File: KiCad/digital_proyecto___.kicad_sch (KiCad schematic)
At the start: 0 parts

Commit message: Poner parte digital
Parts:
- added D1 (x2), D2 (x2), D3 (x2), D4 (x2): RF01VM2S, Diode_SMD:D_SOD-323, symbol Diode:RF01VM2S
- added D5: WS2812B, LED_SMD:LED_WS2812B_PLCC4_5.0x5.0mm_P3.2mm, symbol LED:WS2812B
- added J1 (x2): Conn_01x02, symbol Connector_Generic:Conn_01x02
- added J2, J3: DE9_Pins, symbol Connector:DE9_Pins
- added Q1, Q3 (x2), Q4: PMOS, symbol Simulation_SPICE:PMOS
- added Q1, Q2 (x2), Q4: NMOS, symbol Simulation_SPICE:NMOS
- added R1: 10k, symbol Device:R
- added R2: 330k, symbol Device:R
- added SW1, SW2: SW_SPST, symbol Switch:SW_SPST
- added U1: MCP2551-I-SN, Package_SO:SOIC-8_3.9x4.9mm_P1.27mm, symbol Interface_CAN_LIN:MCP2551-I-SN
- added U2, U3, U4, U5: 74HC04, symbol 74xx:74HC04
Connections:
- new net: Q1.2 (G), U2.2
- new net: Q2.2 (G), U4.2
- new net: Q2.2 (G), U3.2
- new net: R1.1, U1.8 (Rs)
- new net: SW1.2 (B), SW2.1 (A)
- new net: Q4.2 (G), U5.2
- new net: D5.4 (DIN), R2.1
- new net +3.3V: D5.1 (VDD), SW1.1 (A), U1.3 (VDD)
- new net CAN_H: J3.7, U1.7 (CANH)
- new net CAN_L: J3.2, U1.6 (CANL)
- new net CAN_RX: U1.4 (RXD)
- new net CAN_TX: U1.1 (TXD)
- new net GND: D1.2 (A), D2.2 (A), D2.2 (A), D4.2 (A), D5.3 (VSS), J2.5, J3.3, Q1.3 (S), Q2.3 (S), Q2.3 (S), Q4.3 (S), R1.2, U1.2 (VSS)
- new net INA1_M1: Q3.2 (G), U2.1
- new net INA2_M1: Q4.2 (G), U3.1
- new net INB1_M2: Q1.2 (G), U4.1
- new net INB2_M2: Q3.2 (G), U5.1
- new net LED_RGB: R2.2
- new net M1+: D2.1 (K), D3.2 (A), J1.2 (Pin_2), Q1.1 (D), Q3.1 (D), SW2.2 (B)
- new net M1-: D1.1 (K), D4.2 (A), J1.1 (Pin_1), Q2.1 (D), Q4.1 (D)
- new net M2+: D1.2 (A), D2.1 (K), J1.2 (Pin_2), Q1.1 (D), Q2.1 (D)
- new net M2-: D3.2 (A), D4.1 (K), J1.1 (Pin_1), Q3.1 (D), Q4.1 (D)
- new net USART_RX: J2.2
- new net USART_TX: J2.3
- new net V_bat: D1.1 (K), D3.1 (K), D3.1 (K), D4.1 (K), Q1.3 (S), Q3.3 (S), Q3.3 (S), Q4.3 (S)
- no-connect marks 0 -> 14
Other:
- note added: "CANH → DB9 pin 7 CANL → DB9 pin 2 GND → DB9 pin 3"
- note added: "H-BRIDGE 1 (M1)"
- note added: "H-BRIDGE 2 (M2)"
- note added: "LED RGB"
- note added: "Sensor Final de Carrera"
- note added: "TRANSCEIVER CAN"
- note added: "USART"

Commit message: Subida para juntarlo todo 100 por 100
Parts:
- renumbered D4 to D?, D1 to D?, D5 to D?, D2 to D?, D3 to D?, J3 to J?, J1 to J?, J2 to J?, Q3 to Q?, Q2 to Q?, Q4 to Q?, Q1 to Q?, R2 to R?, R1 to R?, SW1 to SW?, SW2 to SW?, U2 to U?, U4 to U?, U1 to U?, U3 to U?, U5 to U?
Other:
- moved on the sheet: D1, D2, D3, D4, D?, J1, J?, Q1, Q2, Q3, Q4, Q?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

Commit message: Actualización ESquematico arreglandolo y corrigiendo fallos
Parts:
- removed SW? (x2): SW_SPST, symbol Switch:SW_SPST
- added C1, C2, C3, C4, C5, C6, C7: 100n, symbol Device:C
- added R3: 120, symbol Device:R
- added R4: 10k, symbol Device:R
- added U6: MAX3232, symbol Interface_UART:MAX3232
- added U7: A1101xLH, Package_TO_SOT_SMD:SOT-23W, symbol Sensor_Magnetic:A1101xLH
- gave numbers to parts that had none: 19
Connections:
- net +3.3V: now also C1.1, C2.1, C3.1, C7.1, R4.1, U6.16 (VCC), U7.1 (V_{CC})
- net CAN_H: now also R3.1
- net CAN_L: now also R3.2
- net GND: now also C1.2, C2.2, C3.2, C7.2, U6.15 (GND), U7.3 (GND)
- net USART_RX: now also U6.13 (R1IN); no longer J2.2
- net USART_TX: now also U6.11 (T1IN); no longer J2.3
- net IN_LED: now reaches D5.4 (DIN), R2.1
- new net: C4.1, U6.1 (C1+)
- new net: C6.1, U6.2 (VS+)
- new net: C4.2, U6.3 (C1-)
- new net: C5.1, U6.4 (C2+)
- new net: C5.2, U6.5 (C2-)
- new net: C6.2, U6.6 (VS-)
- new net MAX_RX: J2.2, U6.12 (R1OUT)
- new net MAX_TX: J2.3, U6.14 (T1OUT)
- new net Sensor_Hall: R4.2, U7.2 (V_{OUT})
- no-connect marks 14 -> 19
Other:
- moved on the sheet: D5, J2, J3, R1, R2, U1

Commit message: Nuevos cambios esquemativo v3
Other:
- note added: "Cada sensor mide el campo magnetico que tiene frente a él. Como piden que el final de carrera sea para el motor del cristal (M1), habra que poner el sensor hall cerca de este motor."
- moved on the sheet: J2
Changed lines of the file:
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@@
 		)
 	)
+	(text "Cada sensor mide el campo magnetico\nque tiene frente a él. Como piden que\nel final de carrera sea para el motor\ndel cristal (M1), habra que poner el \nsensor hall cerca de este motor."
+		(exclude_from_sim no)
+		(at 187.198 42.164 0)
+		(effects
+			(font
+				(size 1.27 1.27)
+			)
+		)
+	)
 	(text "H-BRIDGE 1 (M1)\n"
 		(exclude_from_sim no)
@@
 	)
 	(no_connect
-		(at 39.37 128.27)
+		(at 45.72 130.81)
 	)
 	(no_connect
-		(at 39.37 115.57)
+		(at 45.72 118.11)
 	)
 	(no_connect
-		(at 39.37 130.81)
+		(at 45.72 133.35)
 	)
 	(no_connect
@@
 	)
 	(no_connect
-		(at 39.37 123.19)
+		(at 45.72 125.73)
 	)
 	(no_connect
@@
 	)
 	(no_connect
-		(at 39.37 113.03)
+		(at 45.72 115.57)
 	)
 	(no_connect
@@
 	)
 	(no_connect
-		(at 39.37 118.11)
+		(at 45.72 120.65)
 	)
 	(wire
@@
 	(wire
 		(pts
-			(xy 39.37 110.49) (xy 31.75 110.49)
+			(xy 45.72 113.03) (xy 53.34 113.03)
 		)
 		(stroke
@@
 	(wire
 		(pts
-			(xy 31.75 110.49) (xy 31.75 113.03)
+			(xy 53.34 113.03) (xy 53.34 115.57)
 		)
 		(stroke
@@
 	(global_label "MAX_RX"
 		(shape input)
-		(at 39.37 125.73 180)
+		(at 45.72 128.27 0)
 		(fields_autoplaced yes)
 		(effects
@@
 				(size 1.27 1.27)
 			)
-			(justify right)
+			(justify left)
 		)
 		(property "Intersheetrefs" "${INTERSHEET_REFS}"
-			(at 29.1882 125.73 0)
+			(at 55.9018 128.27 0)
 			(effects
 				(font
 					(size 1.27 1.27)
 				)
-				(justify right)
+				(justify left)
 				(hide yes)
 			)
@@
 	(global_label "MAX_TX"
 		(shape input)
-		(at 39.37 120.65 180)
+		(at 45.72 123.19 0)
 		(fields_autoplaced yes)
 		(effects
@@
 				(size 1.27 1.27)
 			)
-			(justify right)
+			(justify left)
 		)
 		(property "Intersheetrefs" "${INTERSHEET_REFS}"
-			(at 29.4906 120.65 0)
+			(at 55.5994 123.19 0)
 			(effects
 				(font
 					(size 1.27 1.27)
 				)
-				(justify right)
+				(justify left)
 				(hide yes)
 			)
@@
 	(symbol
 		(lib_id "Connector:DE9_Pins")
-		(at 46.99 120.65 0)
+		(at 38.1 123.19 0)
+		(mirror y)
 		(unit 1)
 		(exclude_from_sim no)
@@
 		(fields_autoplaced yes)
 		(property "Reference" "J2"
-			(at 52.07 119.3799 0)
+			(at 33.02 121.9199 0)
 			(effects
 				(font
@@
 		)
 		(property "Value" "DE9_Pins"
-			(at 52.07 121.9199 0)
+			(at 33.02 124.4599 0)
 			(effects
 				(font
@@
 		)
 		(property "Footprint" ""
-			(at 46.99 120.65 0)
+			(at 38.1 123.19 0)
 			(effects
 				(font
@@
 		)
 		(property "Datasheet" "~"
-			(at 46.99 120.65 0)
+			(at 38.1 123.19 0)
 			(effects
 				(font
@@
 		)
 		(property "Description" "9-pin D-SUB connector, pins (male)"
-			(at 46.99 120.65 0)
+			(at 38.1 123.19 0)
 			(effects
 				(font
@@
 	(symbol
 		(lib_id "power:GND")
-		(at 31.75 113.03 0)
+		(at 53.34 115.57 0)
+		(mirror y)
 		(unit 1)
 		(exclude_from_sim no)
@@
 		(fields_autoplaced yes)
 		(property "Reference" "#PWR09"
-			(at 31.75 119.38 0)
+			(at 53.34 121.92 0)
 			(effects
 				(font
@@
 		)
 		(property "Value" "GND"
-			(at 31.75 118.11 0)
+			(at 53.34 120.65 0)
 			(effects
 				(font
@@
 		)
 		(property "Footprint" ""
-			(at 31.75 113.03 0)
+			(at 53.34 115.57 0)
 			(effects
 				(font
@@
 		)
 		(property "Datasheet" ""
-			(at 31.75 113.03 0)
+			(at 53.34 115.57 0)
 			(effects
 				(font
@@
 		)
 		(property "Description" "Power symbol creates a global label with name \"GND\" , ground"
-			(at 31.75 113.03 0)
+			(at 53.34 115.57 0)
 			(effects
 				(font

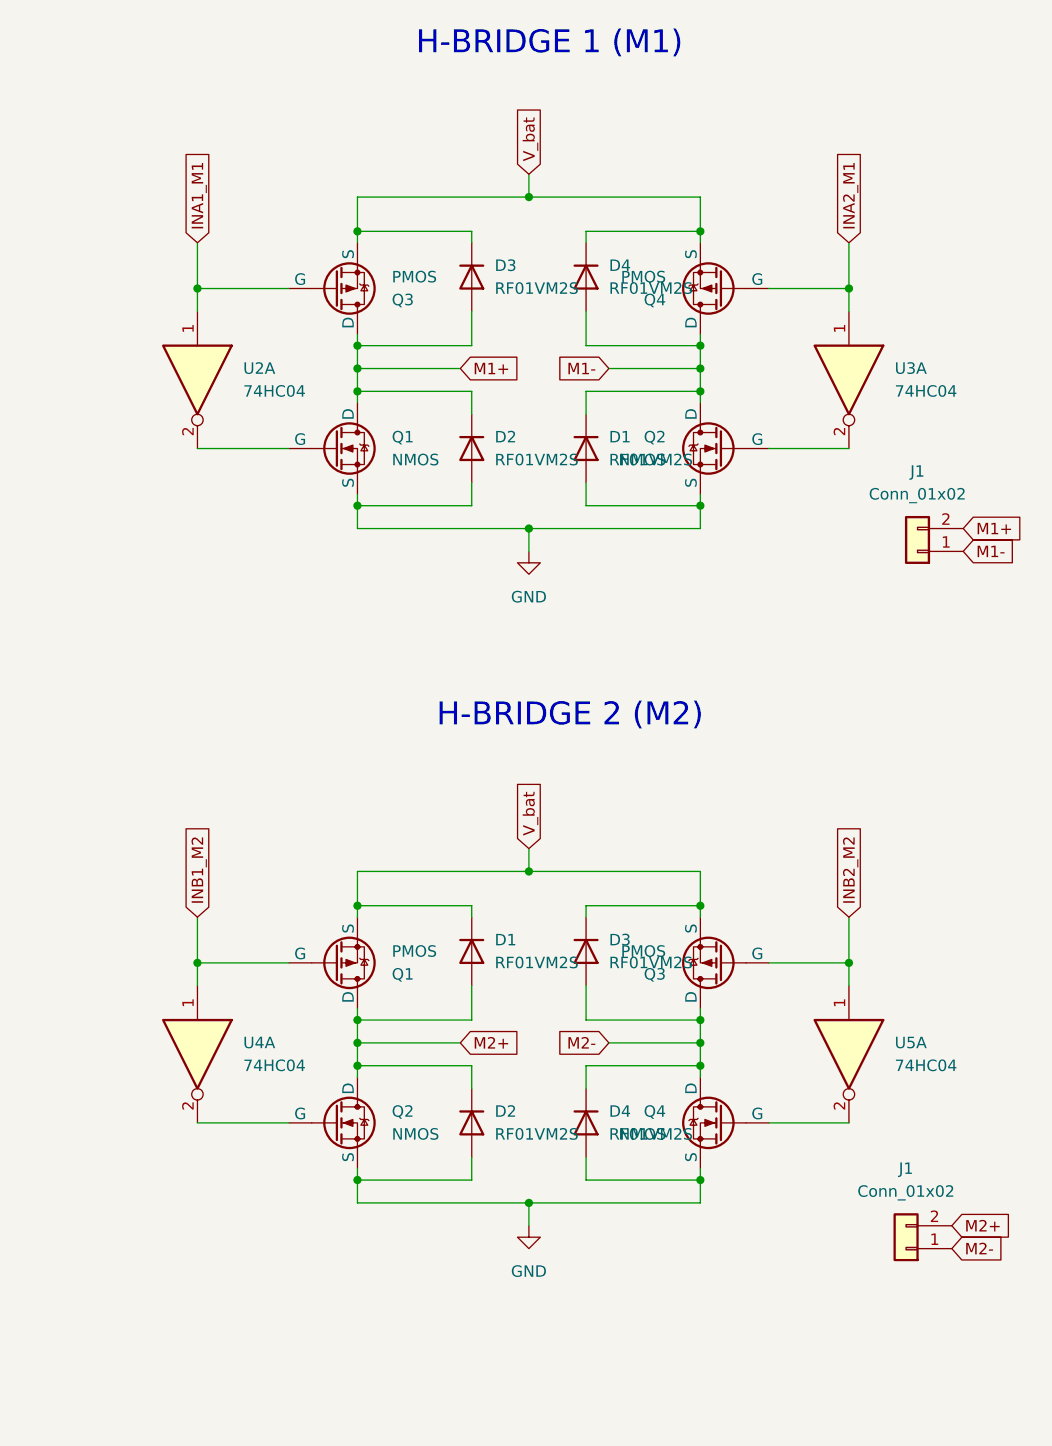
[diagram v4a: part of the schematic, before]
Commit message: Actualización de Esquematico, he puesto footprints y readme cambiado
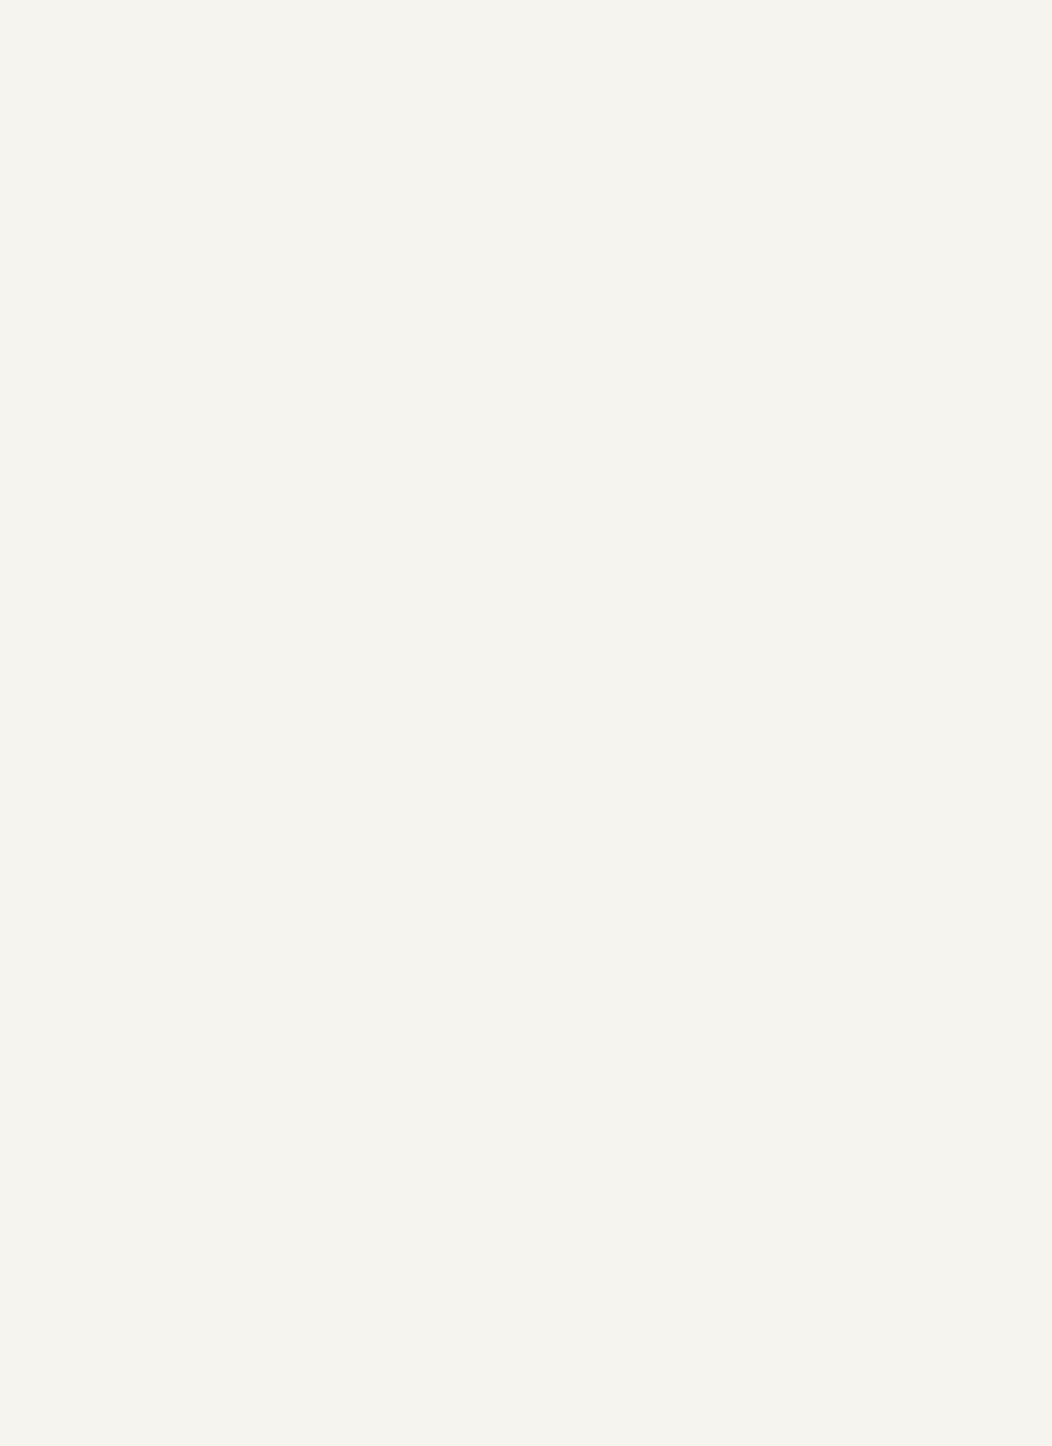
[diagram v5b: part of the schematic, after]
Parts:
- removed D1 (x2), D2 (x2), D3 (x2), D4 (x2): RF01VM2S, Diode_SMD:D_SOD-323, symbol Diode:RF01VM2S
- removed J1 (x2): Conn_01x02, symbol Connector_Generic:Conn_01x02
- removed Q1, Q3 (x2), Q4: PMOS, symbol Simulation_SPICE:PMOS
- removed Q1, Q2 (x2), Q4: NMOS, symbol Simulation_SPICE:NMOS
- removed U2, U3, U4, U5: 74HC04, symbol 74xx:74HC04
- C1, C2, C3, C4, C5, C6, C7: footprint (none) -> Capacitor_SMD:C_0805_2012Metric
- J2, J3: footprint (none) -> Connector_Dsub:DSUB-9_Socket_Horizontal_P2.77x2.84mm_EdgePinOffset4.94mm_Housed_MountingHolesOffset4.94mm
- R1, R2, R3, R4: footprint (none) -> Resistor_SMD:R_0805_2012Metric
- U6: footprint (none) -> Package_SO:SSOP-16_5.3x6.2mm_P0.65mm
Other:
- note removed: "H-BRIDGE 1 (M1)"
- note removed: "H-BRIDGE 2 (M2)"

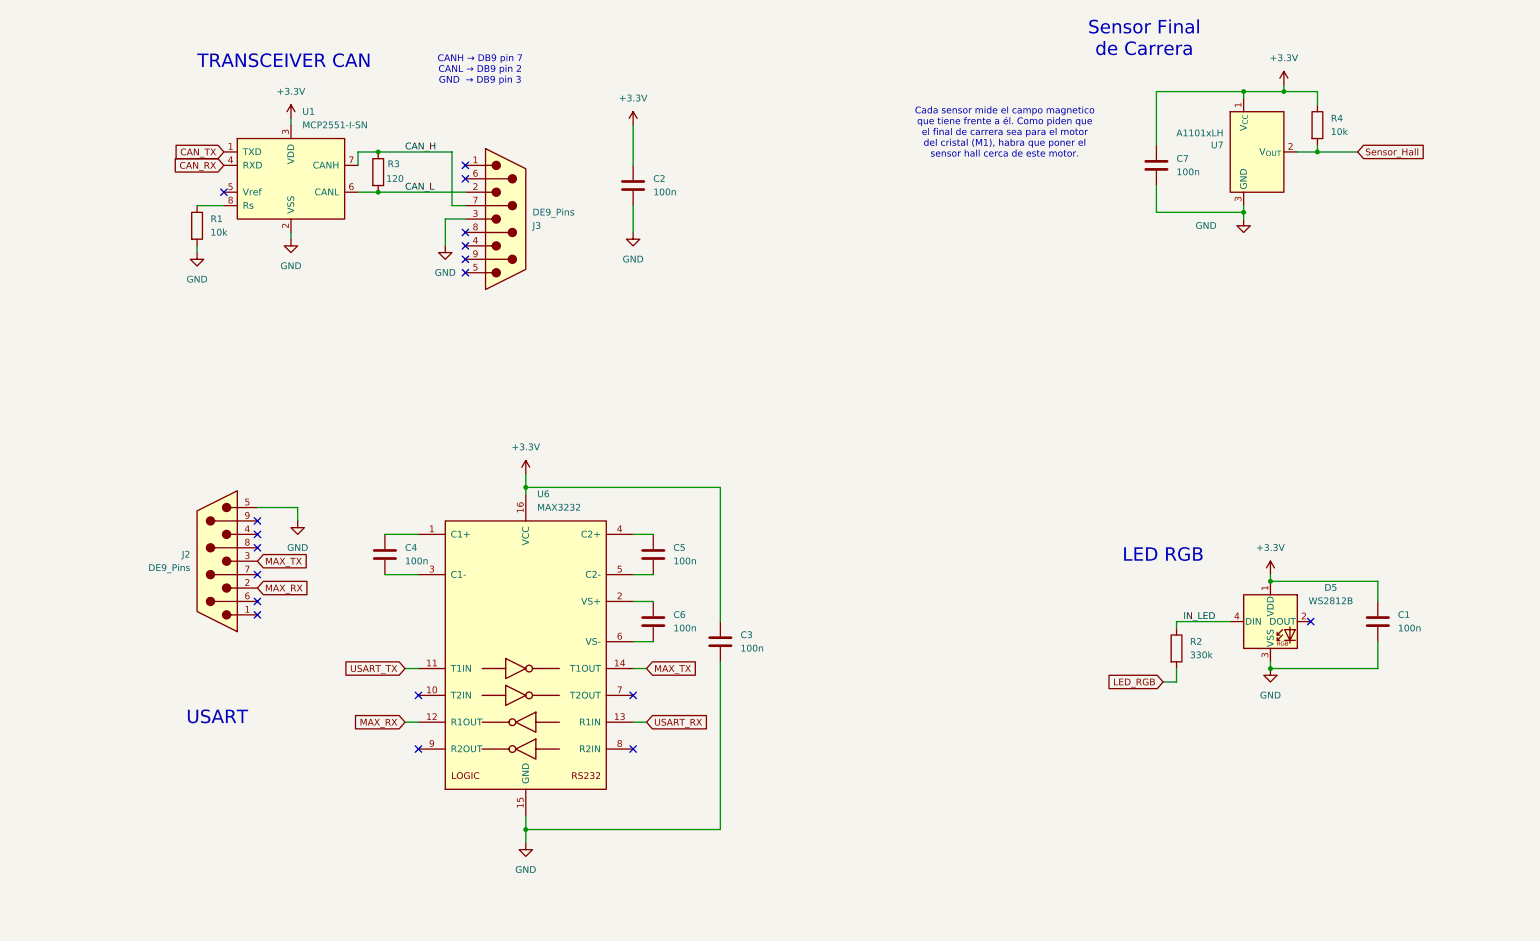
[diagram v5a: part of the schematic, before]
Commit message: Esquematico cambio en Sensor final de Carrera y Readme
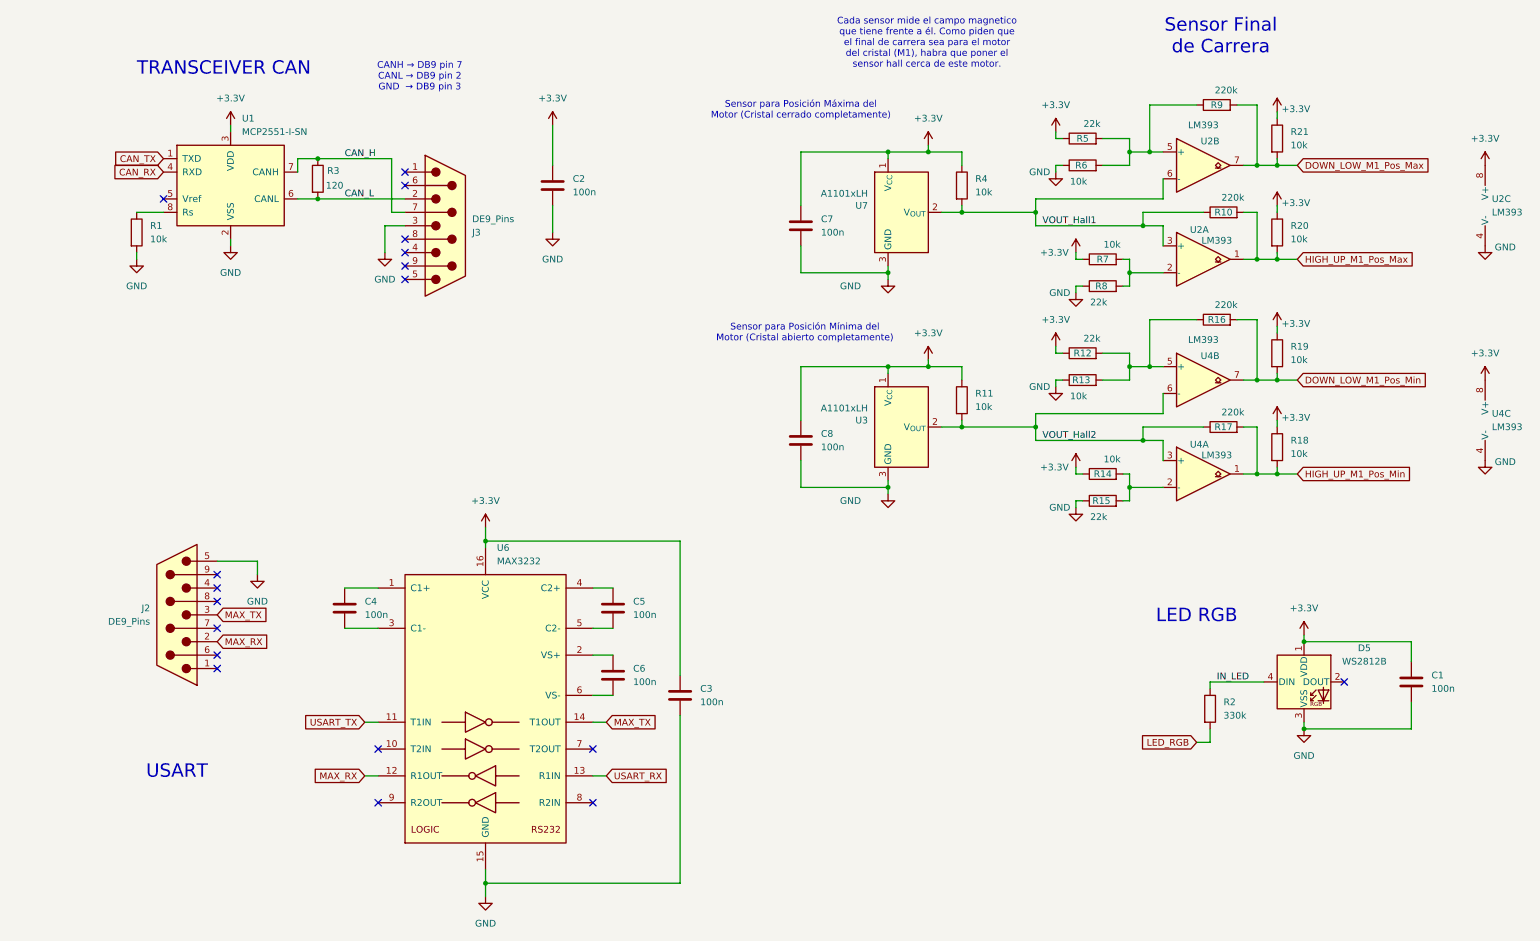
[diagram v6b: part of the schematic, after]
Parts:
- added C8: 100n, Capacitor_SMD:C_0805_2012Metric, symbol Device:C
- added R10, R16, R17, R9: 220k, Resistor_SMD:R_0805_2012Metric, symbol Device:R
- added R11, R13, R14, R18, R19, R20, R21, R6, R7: 10k, Resistor_SMD:R_0805_2012Metric, symbol Device:R
- added R12, R15, R5, R8: 22k, Resistor_SMD:R_0805_2012Metric, symbol Device:R
- added U2, U4: LM393, Package_SO:SOIC-8_5.3x6.2mm_P1.27mm, symbol Comparator:LM393
- added U3: A1101xLH, Package_TO_SOT_SMD:SOT-23W, symbol Sensor_Magnetic:A1101xLH
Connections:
- net +3.3V: now also C8.1, R11.1, R12.1, R14.1, R18.1, R19.1, R20.1, R21.1, R5.1, R7.1, U2.8 (V+), U3.1 (V_{CC}), U4.8 (V+)
- net GND: now also C8.2, R13.1, R15.1, R6.1, R8.1, U2.4 (V-), U3.3 (GND), U4.4 (V-)
- net Sensor_Hall renamed VOUT_Hall1
- net VOUT_Hall1: now also R10.1, U2.3 (+), U2.6 (-)
- new net: R7.2, R8.2, U2.2 (-)
- new net: R12.2, R13.2, R16.1, U4.5 (+)
- new net: R5.2, R6.2, R9.1, U2.5 (+)
- new net: R14.2, R15.2, U4.2 (-)
- new net DOWN_LOW_M1_Pos_Max: R21.2, R9.2, U2.7
- new net DOWN_LOW_M1_Pos_Min: R16.2, R19.2, U4.7
- new net HIGH_UP_M1_Pos_Max: R10.2, R20.2, U2.1
- new net HIGH_UP_M1_Pos_Min: R17.2, R18.2, U4.1
- new net VOUT_Hall2: R11.2, R17.1, U3.2 (V_{OUT}), U4.3 (+), U4.6 (-)
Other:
- note added: "Sensor para Posición Máxima del Motor (Cristal cerrado completamente)"
- note added: "Sensor para Posición Mínima del Motor (Cristal abierto completamente)"
- moved on the sheet: C1, C2, C3, C4, C5, C6, C7, D5, J2, J3, R1, R2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
